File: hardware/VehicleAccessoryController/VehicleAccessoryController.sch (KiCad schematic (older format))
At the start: 10 parts, among them J501 Conn_01x03, P501 TC2030-MCP, U101 REM30-2405SW, U102 ATMEGA328P-M(32QFN_MLF)

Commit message: Schematic additions
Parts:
- added D201: LED_ALT, symbol Device:LED_ALT
- added F401: Fuse, symbol Device:Fuse
- added J502: Front Conn, symbol Connector:Screw_Terminal_01x03
- added J503: Rear Conn, symbol Connector:Screw_Terminal_01x03
- added J504: Left Conn, symbol Connector:Screw_Terminal_01x03
- added J505: Right Conn, symbol Connector:Screw_Terminal_01x03
- added R703: 22R, symbol Device:R
- added fid2, fid3: FID, VehicleAccessoryController:Fiducial, symbol VehicleAccessoryController:FID
- C802, C803: footprint (none) -> VehicleAccessoryController:C_0603
- J501: value Conn_01x03 -> Input
- P601: renamed from P501; footprint (none) -> Tag-Connect:TC2030_SMALL
- R701: value R -> 48k7
- R702: footprint (none) -> VehicleAccessoryController:R_0603
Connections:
- net labels added: +12VA, ACC, CTRL, GNDA, PARK, STATUS, TRIM
- net labels removed: +12V
- wire segments 31 -> 76
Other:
- note added: ">1/16W"
- note added: "Voutnom | R1 | R2 | Ku | Vref\n 5VDC | 5k1Ω | 2kΩ | 2.5 | 2.5VDC\n\n | R1 x Vref |\nRup =|---------------| - R2\n | Voutset - Vref - Ku |\n\n | 5k1 x 2.5 |\nRup =|---------------| - 2k\n | 5.25 - 2.5 - 2.5 |\n\nRup = 49kΩ ~~ Closest E96 = 48k7Ω"
- moved on the sheet: C801, C802, C803, J501, P601, R701, R702, U101, U102, fid1

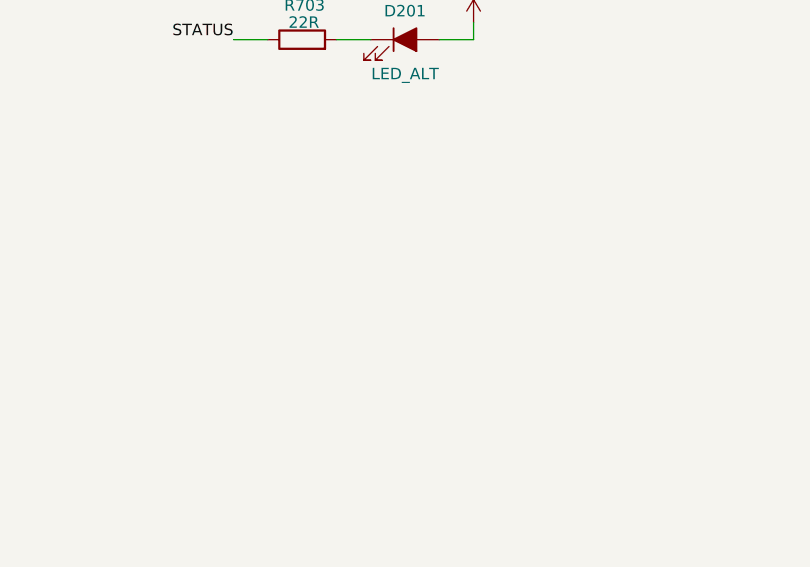
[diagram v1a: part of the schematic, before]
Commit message: Schematic additions
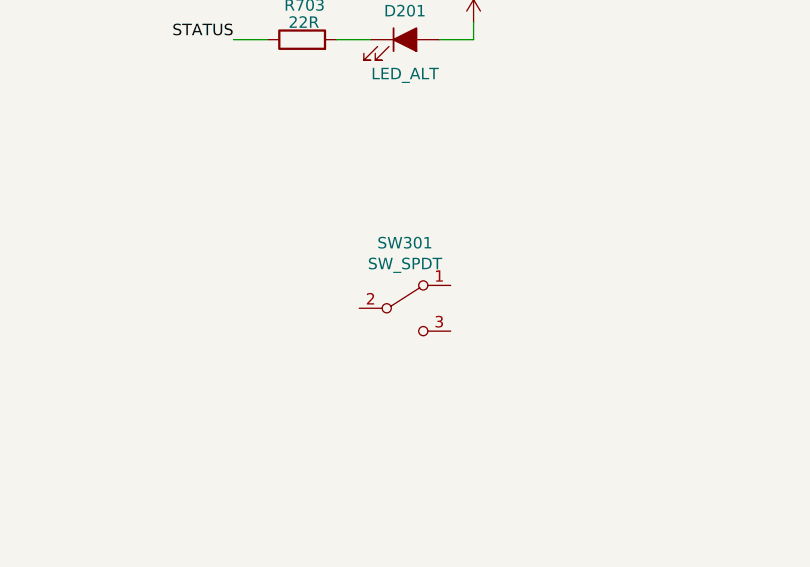
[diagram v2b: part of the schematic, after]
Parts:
- added SW301: SW_SPDT, symbol Switch:SW_SPDT
- F401: footprint (none) -> VehicleAccessoryController:Littelfuse_01530007
- J502, J503, J504, J505: footprint (none) -> VehicleAccessoryController:Keystone_8719
- R701, R703: footprint (none) -> VehicleAccessoryController:R_0603
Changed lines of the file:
@@
 F 0 "R701" H 3795 1646 50  0000 L CNN
 F 1 "48k7" H 3795 1555 50  0000 L CNN
-F 2 "" V 3655 1600 50  0001 C CNN
+F 2 "VehicleAccessoryController:R_0603" V 3655 1600 50  0001 C CNN
 F 3 "~" H 3725 1600 50  0001 C CNN
 	1    3725 1600
@@
 F 0 "F401" V 2125 1475 50  0000 L CNN
 F 1 "Fuse" V 2050 1475 50  0000 L CNN
-F 2 "" V 1905 1550 50  0001 C CNN
+F 2 "VehicleAccessoryController:Littelfuse_01530007" V 1905 1550 50  0001 C CNN
 F 3 "~" H 1975 1550 50  0001 C CNN
 	1    1975 1550
@@
 F 0 "J502" H 9400 2625 50  0000 L CNN
 F 1 "Front Conn" V 9625 2225 50  0000 L CNN
-F 2 "" H 9525 2425 50  0001 C CNN
+F 2 "VehicleAccessoryController:Keystone_8719" H 9525 2425 50  0001 C CNN
 F 3 "~" H 9525 2425 50  0001 C CNN
 	1    9525 2425
@@
 F 0 "J503" H 9400 3425 50  0000 L CNN
 F 1 "Rear Conn" V 9625 3050 50  0000 L CNN
-F 2 "" H 9525 3225 50  0001 C CNN
+F 2 "VehicleAccessoryController:Keystone_8719" H 9525 3225 50  0001 C CNN
 F 3 "~" H 9525 3225 50  0001 C CNN
 	1    9525 3225
@@
 F 0 "J504" H 9400 4225 50  0000 L CNN
 F 1 "Left Conn" V 9625 3850 50  0000 L CNN
-F 2 "" H 9525 4025 50  0001 C CNN
+F 2 "VehicleAccessoryController:Keystone_8719" H 9525 4025 50  0001 C CNN
 F 3 "~" H 9525 4025 50  0001 C CNN
 	1    9525 4025
@@
 F 0 "J505" H 9400 5025 50  0000 L CNN
 F 1 "Right Conn" V 9625 4600 50  0000 L CNN
-F 2 "" H 9525 4825 50  0001 C CNN
+F 2 "VehicleAccessoryController:Keystone_8719" H 9525 4825 50  0001 C CNN
 F 3 "~" H 9525 4825 50  0001 C CNN
 	1    9525 4825
@@
 F 0 "R703" V 2650 3925 50  0000 L CNN
 F 1 "22R" V 2575 3950 50  0000 L CNN
-F 2 "" V 2430 4025 50  0001 C CNN
+F 2 "VehicleAccessoryController:R_0603" V 2430 4025 50  0001 C CNN
 F 3 "~" H 2500 4025 50  0001 C CNN
 	1    2500 4025
@@
 Text Label 9175 4825 2    50   ~ 0
 PARK
+$Comp
+L Switch:SW_SPDT SW301
+U 1 1 5DB3F551
+P 2950 5200
+F 0 "SW301" H 2950 5485 50  0000 C CNN
+F 1 "SW_SPDT" H 2950 5394 50  0000 C CNN
+F 2 "" H 2950 5200 50  0001 C CNN
+F 3 "" H 2950 5200 50  0001 C CNN
+	1    2950 5200
+	1    0    0    -1
+$EndComp
 $EndSCHEMATC

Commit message: schematic additions
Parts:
- removed U101: REM30-2405SW, VehicleAccessoryController:REM30-XXXXXW, symbol VehicleAccessoryController:REM30-2405SW
- added C804: 0.1uF, VehicleAccessoryController:C_0603, symbol Device:C
- added R703: 2M43, VehicleAccessoryController:R_0603, symbol Device:R
- added R704: 84k5, VehicleAccessoryController:R_0603, symbol Device:R
- added R705: 49k9, VehicleAccessoryController:R_0603, symbol Device:R
- added R? (x4): 30k5, VehicleAccessoryController:R_0603, symbol Device:R
- added U101: RECOM_REMX0-W, VehicleAccessoryController:REM20-XXXXXW, symbol VehicleAccessoryController:RECOM_REMX0-W
- added U103: TPS3710, VehicleAccessoryController:TI DSE (S-PWSON-N6), symbol VehicleAccessoryController:TPS3710
- D201: footprint (none) -> VehicleAccessoryController:LED_0603
- J501: footprint (none) -> VehicleAccessoryController:Keystone_8719
- R706: renamed from R703; value 22R -> 160R
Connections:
- net +12VA: now also C804.1, R703.2, R705.1, U103.2 (VDD)
- net +5V: now also U101.6 (+Vout)
- net CTRL: now also R705.2, U101.3 (CTRL), U103.6 (OUT)
- net GND: now also R?.1, R?.1, R?.1, R?.1, U101.5 (-Vout)
- net GNDA: now also C804.2, R704.1, U101.2 (-Vin), U103.1 (GND), U103.3 (GND), U103.5 (GND)
- net PARK: no longer J502.2 (Pin_2), J503.2 (Pin_2), J504.2 (Pin_2), J505.2 (Pin_2)
- net TRIM: now also U101.4 (Trim)
- net at F401.2: now also U101.1 (+Vin)
- new net: J502.2 (Pin_2), R?.2
- new net: J503.2 (Pin_2), R?.2
- new net: J504.2 (Pin_2), R?.2
- new net: J505.2 (Pin_2), R?.2
- new net: R703.1, R704.2, U103.4 (SENSE)
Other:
- note added: "Active Low"
- note added: "SI8710CC-B-IS"
- note added: "| R1 |\nVmon(uv) = | 1 + ----| x Vit-\n | R2 |\n\n | 2M43|\nVmon(uv) = | 1 + ----| x 394.5mV\n | 84k5 |\n\nVmon(uv) = 11.739V"
- moved on the sheet: D201, J502, J503, J504, J505, R706, SW301

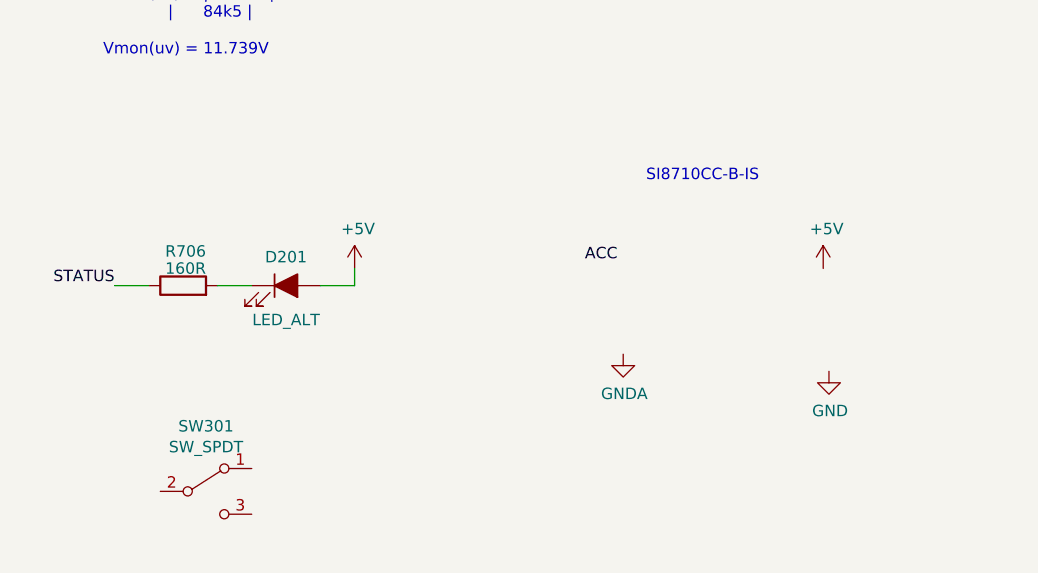
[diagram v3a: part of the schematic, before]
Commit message: Schematic updates
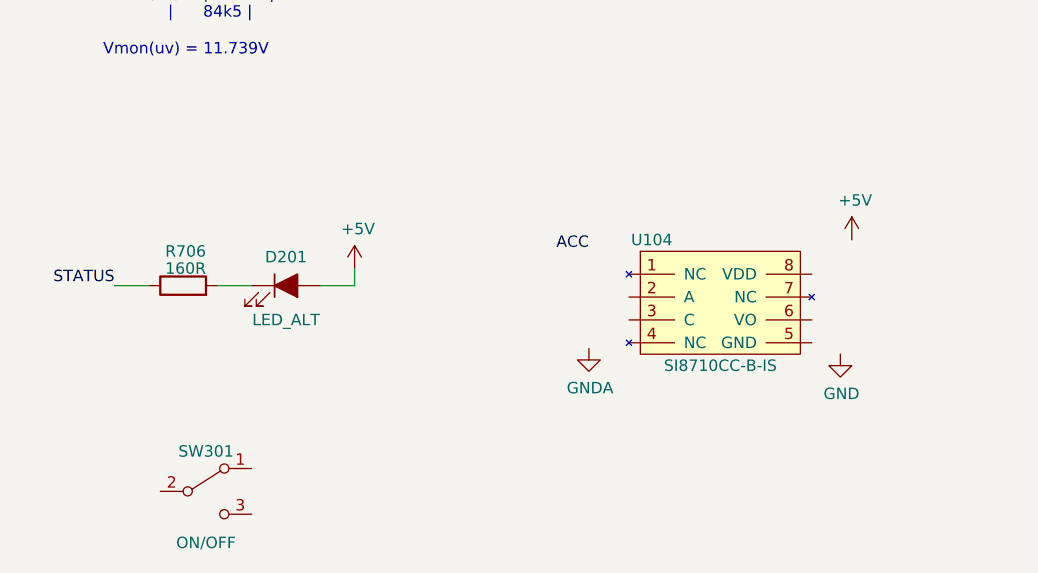
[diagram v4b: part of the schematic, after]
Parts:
- added U104: SI8710CC-B-IS, symbol VehicleAccessoryController:SI8710CC-B-IS
- SW301: value SW_SPDT -> ON/OFF
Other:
- note removed: "SI8710CC-B-IS"
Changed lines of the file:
@@
 Sheet 1 1
 Title "Vehicle Accessory Controller"
-Date "2019-10-27"
+Date "2019-10-29"
 Rev "0.1"
 Comp "Noctivore"
@@
 U 1 1 5DB3F551
 P 2625 7350
-F 0 "SW301" H 2625 7635 50  0000 C CNN
-F 1 "SW_SPDT" H 2625 7544 50  0000 C CNN
+F 0 "SW301" H 2625 7525 50  0000 C CNN
+F 1 "ON/OFF" H 2625 7125 50  0000 C CNN
 F 2 "" H 2625 7350 50  0001 C CNN
 F 3 "" H 2625 7350 50  0001 C CNN
@@
 $EndComp
 $Comp
-L power:GND #PWR?
+L power:GND #PWR0125
 U 1 1 5DB690C0
 P 8950 1975
-F 0 "#PWR?" H 8950 1725 50  0001 C CNN
+F 0 "#PWR0125" H 8950 1725 50  0001 C CNN
 F 1 "GND" H 8955 1802 50  0000 C CNN
 F 2 "" H 8950 1975 50  0001 C CNN
@@
 $EndComp
 $Comp
-L power:GND #PWR?
+L power:GND #PWR0126
 U 1 1 5DB78A2C
 P 8950 3075
-F 0 "#PWR?" H 8950 2825 50  0001 C CNN
+F 0 "#PWR0126" H 8950 2825 50  0001 C CNN
 F 1 "GND" H 8955 2902 50  0000 C CNN
 F 2 "" H 8950 3075 50  0001 C CNN
@@
 $EndComp
 $Comp
-L power:GND #PWR?
+L power:GND #PWR0127
 U 1 1 5DB825A5
 P 8950 4175
-F 0 "#PWR?" H 8950 3925 50  0001 C CNN
+F 0 "#PWR0127" H 8950 3925 50  0001 C CNN
 F 1 "GND" H 8955 4002 50  0000 C CNN
 F 2 "" H 8950 4175 50  0001 C CNN
@@
 $EndComp
 $Comp
-L power:GND #PWR?
+L power:GND #PWR0128
 U 1 1 5DB8C5A1
 P 8950 5275
-F 0 "#PWR?" H 8950 5025 50  0001 C CNN
+F 0 "#PWR0128" H 8950 5025 50  0001 C CNN
 F 1 "GND" H 8955 5102 50  0000 C CNN
 F 2 "" H 8950 5275 50  0001 C CNN
@@
 Wire Wire Line
 	9250 5000 9250 5275
-Text Notes 4550 6000 0    50   ~ 0
-SI8710CC-B-IS
-Text Label 4425 6350 2    50   ~ 0
+Text Label 4300 6300 2    50   ~ 0
 ACC
 $Comp
-L power:GNDA #PWR?
+L power:GNDA #PWR0129
 U 1 1 5DB94C72
-P 4450 6750
-F 0 "#PWR?" H 4450 6500 50  0001 C CNN
-F 1 "GNDA" H 4455 6577 50  0000 C CNN
-F 2 "" H 4450 6750 50  0001 C CNN
-F 3 "" H 4450 6750 50  0001 C CNN
-	1    4450 6750
-	1    0    0    -1
-$EndComp
-$Comp
-L power:+5V #PWR?
+P 4300 6725
+F 0 "#PWR0129" H 4300 6475 50  0001 C CNN
+F 1 "GNDA" H 4305 6552 50  0000 C CNN
+F 2 "" H 4300 6725 50  0001 C CNN
+F 3 "" H 4300 6725 50  0001 C CNN
+	1    4300 6725
+	1    0    0    -1
+$EndComp
+$Comp
+L power:+5V #PWR0130
 U 1 1 5DB94CF1
-P 5325 6375
-F 0 "#PWR?" H 5325 6225 50  0001 C CNN
-F 1 "+5V" H 5340 6548 50  0000 C CNN
-F 2 "" H 5325 6375 50  0001 C CNN
-F 3 "" H 5325 6375 50  0001 C CNN
-	1    5325 6375
-	1    0    0    -1
-$EndComp
-$Comp
-L power:GND #PWR?
+P 5450 6250
+F 0 "#PWR0130" H 5450 6100 50  0001 C CNN
+F 1 "+5V" H 5465 6423 50  0000 C CNN
+F 2 "" H 5450 6250 50  0001 C CNN
+F 3 "" H 5450 6250 50  0001 C CNN
+	1    5450 6250
+	1    0    0    -1
+$EndComp
+$Comp
+L power:GND #PWR0131
 U 1 1 5DB94D36
-P 5350 6825
-F 0 "#PWR?" H 5350 6575 50  0001 C CNN
-F 1 "GND" H 5355 6652 50  0000 C CNN
-F 2 "" H 5350 6825 50  0001 C CNN
-F 3 "" H 5350 6825 50  0001 C CNN
-	1    5350 6825
-	1    0    0    -1
-$EndComp
+P 5400 6750
+F 0 "#PWR0131" H 5400 6500 50  0001 C CNN
+F 1 "GND" H 5405 6577 50  0000 C CNN
+F 2 "" H 5400 6750 50  0001 C CNN
+F 3 "" H 5400 6750 50  0001 C CNN
+	1    5400 6750
+	1    0    0    -1
+$EndComp
+$Comp
+L VehicleAccessoryController:SI8710CC-B-IS U104
+U 1 1 5DB926C2
+P 4875 6550
+F 0 "U104" H 4575 6850 50  0000 C CNN
+F 1 "SI8710CC-B-IS" H 4875 6300 50  0000 C CNN
+F 2 "" H 4875 6550 50  0001 C CNN
+F 3 "" H 4875 6550 50  0001 C CNN
+	1    4875 6550
+	1    0    0    -1
+$EndComp

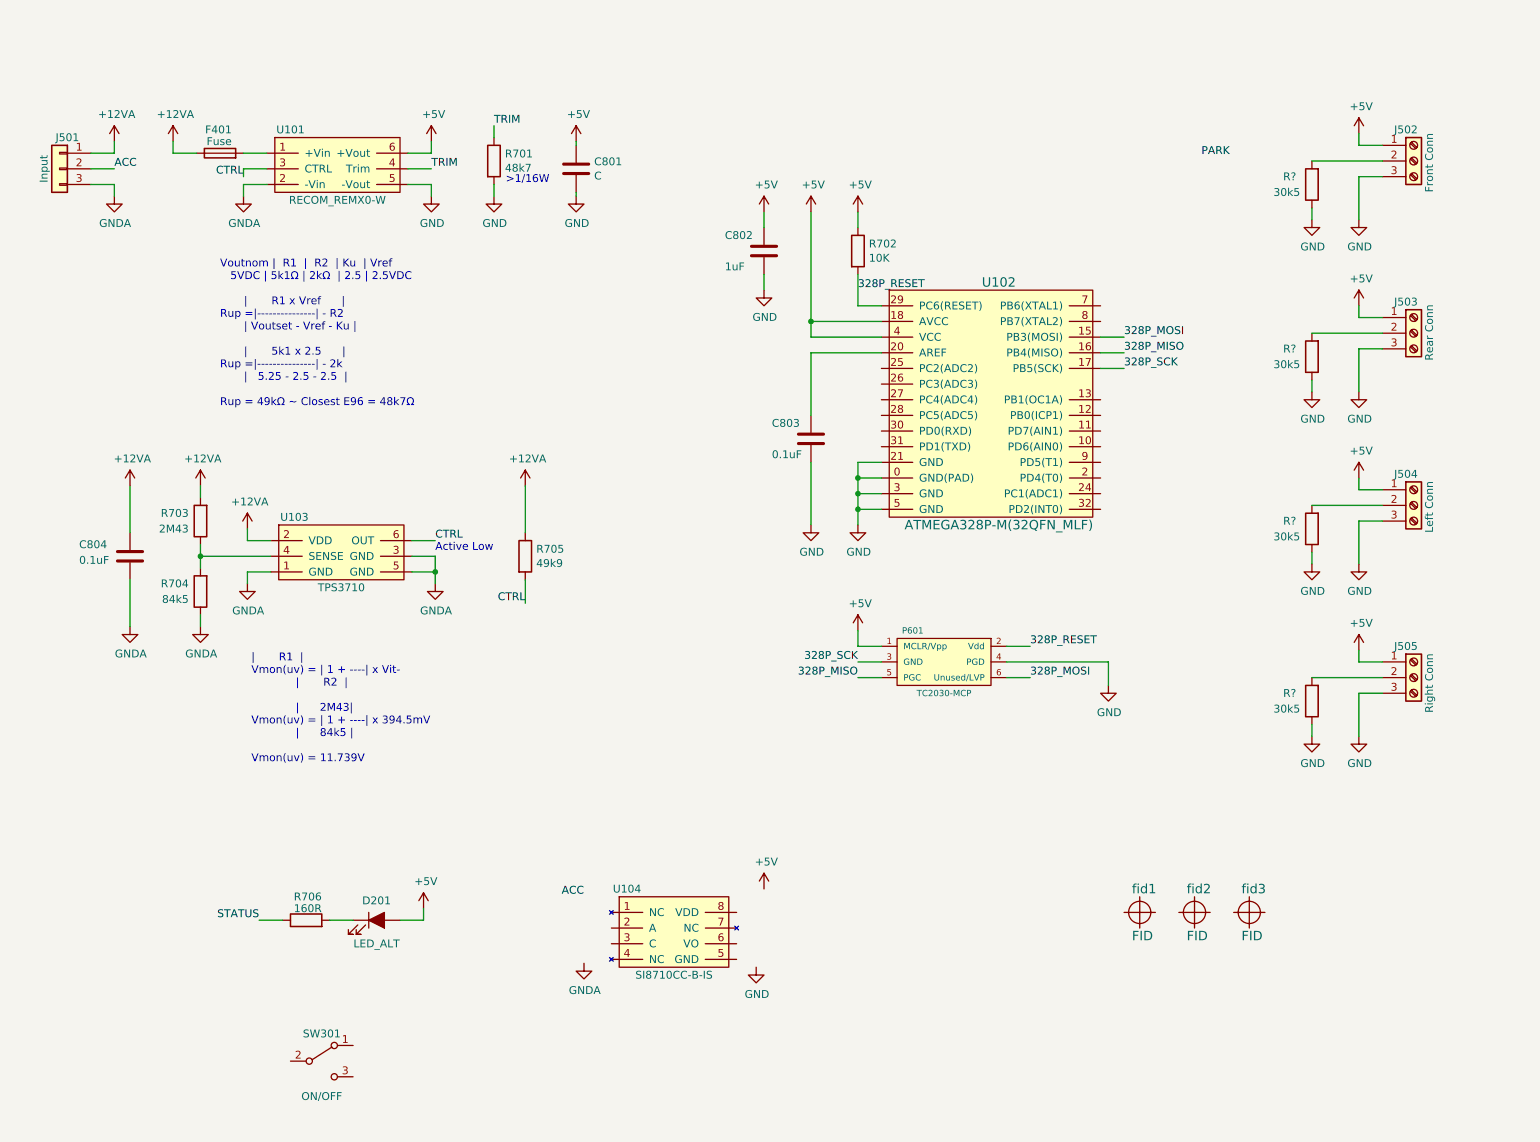
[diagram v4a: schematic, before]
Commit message: Schematic updates
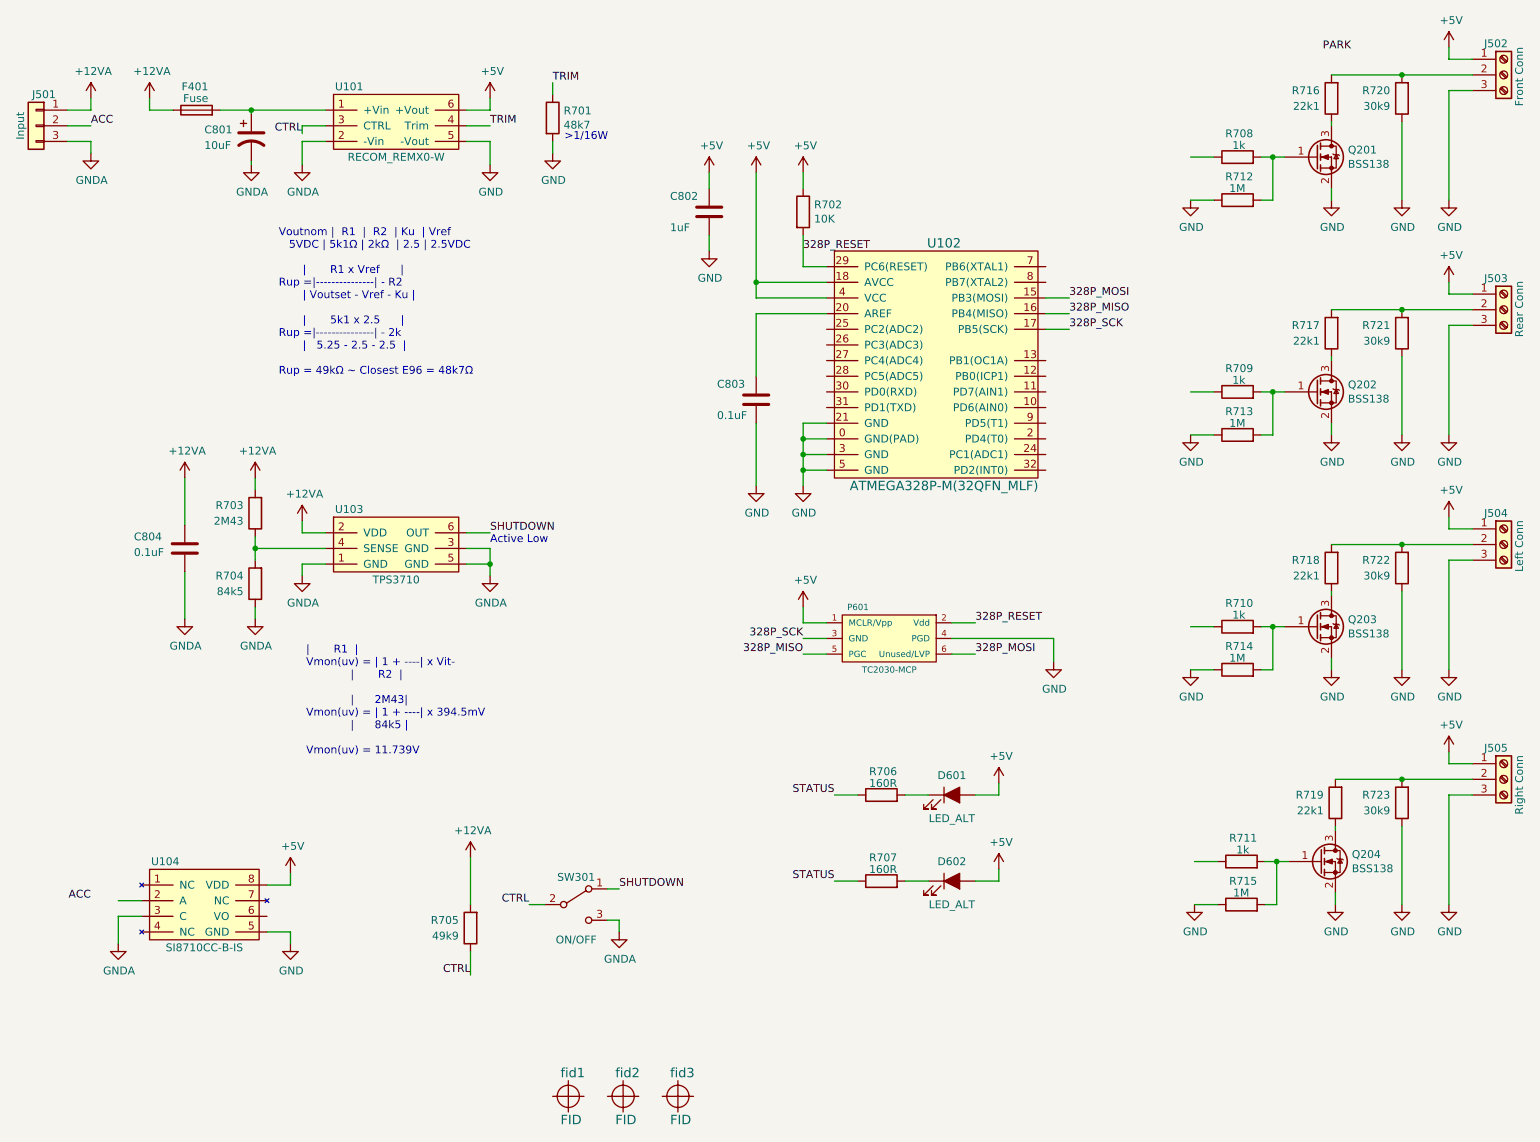
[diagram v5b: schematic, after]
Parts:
- removed C801: C, symbol Device:C
- added C801: 10uF, VehicleAccessoryController:C_2917_D, symbol Device:CP1
- added D602: LED_ALT, VehicleAccessoryController:LED_0603, symbol Device:LED_ALT
- added Q201, Q202, Q203, Q204: BSS138, Package_TO_SOT_SMD:SOT-23, symbol Transistor_FET:BSS138
- added R707: 160R, VehicleAccessoryController:R_0603, symbol Device:R
- added R708, R709, R710, R711: 1k, VehicleAccessoryController:R_0603, symbol Device:R
- added R712, R713, R714, R715: 1M, VehicleAccessoryController:R_0603, symbol Device:R
- added R716, R717, R718, R719: 22k1, VehicleAccessoryController:R_0603, symbol Device:R
- R720, R721, R722, R723: renamed from R?; value 30k5 -> 30k9
- renumbered D201 to D601
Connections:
- net labels added: SHUTDOWN
- wire segments 98 -> 150
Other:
- moved on the sheet: C802, C803, C804, D601, F401, J501, J502, J503, J504, J505, P601, R701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
